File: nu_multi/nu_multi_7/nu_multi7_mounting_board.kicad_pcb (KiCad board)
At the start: 2 copper layers, 82.5 x 18.2 mm, 16 parts, among them J1 CONN_01X02, J10 CONN_01X03, J11 CONN_01X02, J12 CONN_01X03, J13 CONN_01X02, J14 CONN_01X03, J15 CONN_01X14, J2 CONN_01X03, J3 CONN_01X02, J4 CONN_01X02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

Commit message: Updates; added nu multi-8 mounting board
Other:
- board text added: "v2.5"

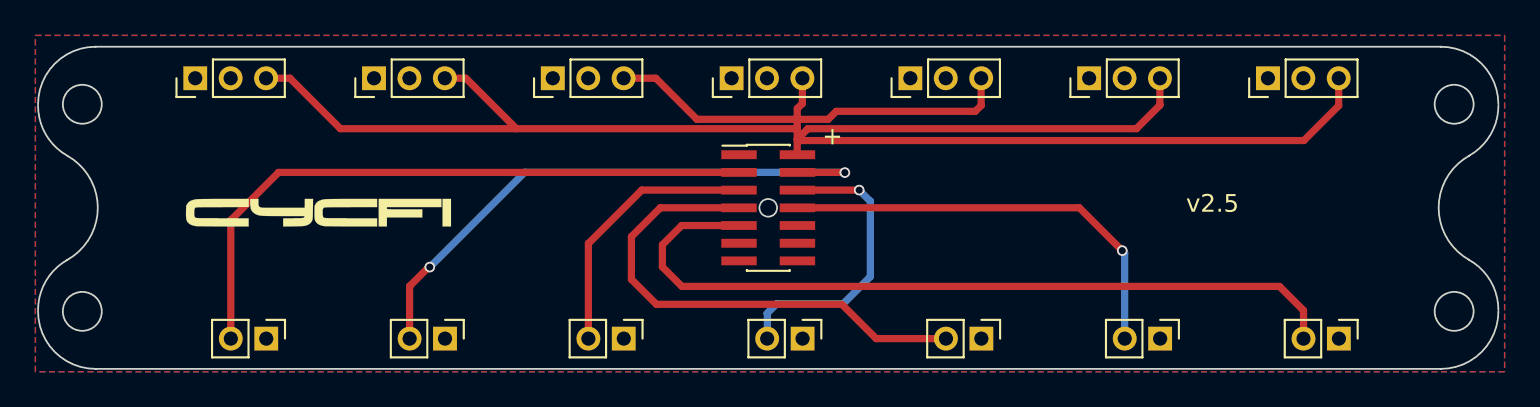
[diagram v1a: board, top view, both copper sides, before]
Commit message: Upgraded schematics and PCB layout using Nu Capsule footprint
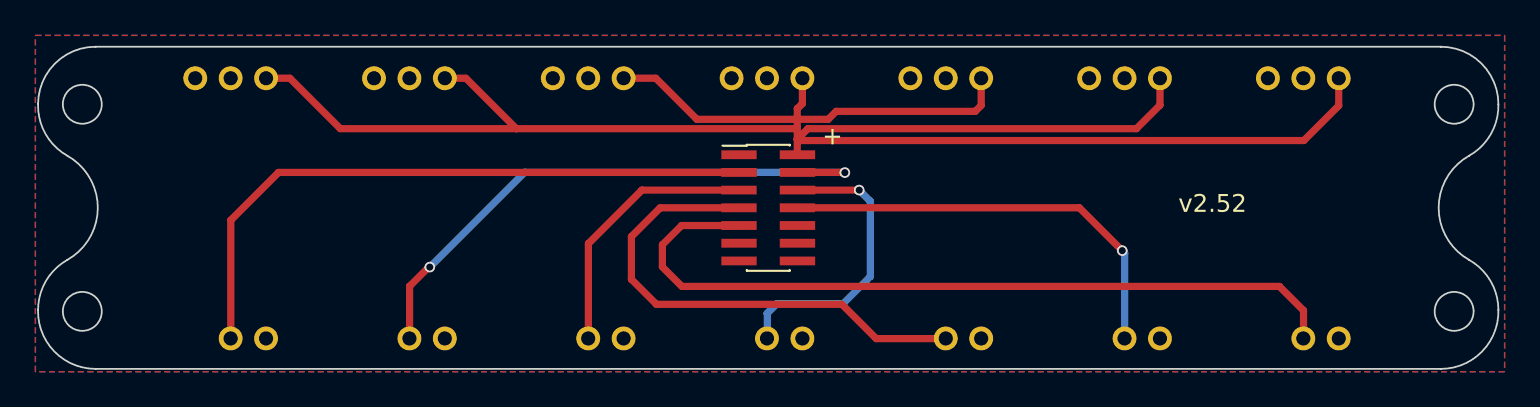
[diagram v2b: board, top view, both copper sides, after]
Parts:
- removed G***: LOGO, Symbols:Cycfi_Logo
- removed J1, J11, J13, J3, J4, J7, J9: CONN_01X02, Pin_Headers:Pin_Header_Straight_1x02_Pitch2.00mm
- removed J10, J12, J14, J2, J5, J6, J8: CONN_01X03, Pin_Headers:Pin_Header_Straight_1x03_Pitch2.00mm
- added U1: nu_capsule, cycfi_library:nu_capsule, F.Cu at (116.0, 62.4)
- added U2: nu_capsule, cycfi_library:nu_capsule, F.Cu at (126.1, 62.4)
- added U3: nu_capsule, cycfi_library:nu_capsule, F.Cu at (136.2, 62.4)
- added U4: nu_capsule, cycfi_library:nu_capsule, F.Cu at (146.3, 62.4)
- added U5: nu_capsule, cycfi_library:nu_capsule, F.Cu at (156.4, 62.4)
- added U6: nu_capsule, cycfi_library:nu_capsule, F.Cu at (166.5, 62.4)
- added U7: nu_capsule, cycfi_library:nu_capsule, F.Cu at (176.6, 62.4)
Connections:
- J15 pad 10: Net-(J15-Pad10) -> unconnected-(J15-Pad10)
- J15 pad 3: Net-(J13-Pad2) -> CH1
- J15 pad 4: Net-(J11-Pad2) -> CH2
- J15 pad 5: Net-(J15-Pad5) -> CH3
- J15 pad 6: Net-(J15-Pad6) -> CH4
- J15 pad 7: Net-(J15-Pad7) -> CH5
- J15 pad 8: Net-(J15-Pad8) -> CH6
- J15 pad 9: Net-(J1-Pad2) -> CH7
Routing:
- net CH7: track 0.00 -> 44.9 mm
- net Net-(J1-Pad2): track 44.9 -> 0.00 mm
- net Net-(J13-Pad2): track 36.5 -> 0.00 mm
- net CH1: track 0.00 -> 36.5 mm
- net Net-(J11-Pad2): track 32.9 -> 0.00 mm, vias 2 -> 0
- net CH2: track 0.00 -> 32.9 mm, vias 0 -> 2
- net Net-(J15-Pad7): track 28.3 -> 0.00 mm
- net CH5: track 0.00 -> 28.3 mm
- net Net-(J15-Pad8): track 24.4 -> 0.00 mm, vias 1 -> 0
- net CH6: track 0.00 -> 24.4 mm, vias 0 -> 1
- net Net-(J15-Pad6): track 16.8 -> 0.00 mm, vias 1 -> 0
- net CH4: track 0.00 -> 16.8 mm, vias 0 -> 1
- net Net-(J15-Pad5): track 15.1 -> 0.00 mm
- net CH3: track 0.00 -> 15.1 mm
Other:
- outline, holes or cut-outs redrawn
- net class Default removed
- board text added: "v2.52"
- board text removed: "v2.5"

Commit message: Use 2x7p connector from cycfi lib
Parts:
- J15: footprint Pin_Headers:Pin_Header_Straight_2x07_Pitch1.00mm_SMD -> cycfi_library:pin_header_2x7p_1.00mm_smd_vertical

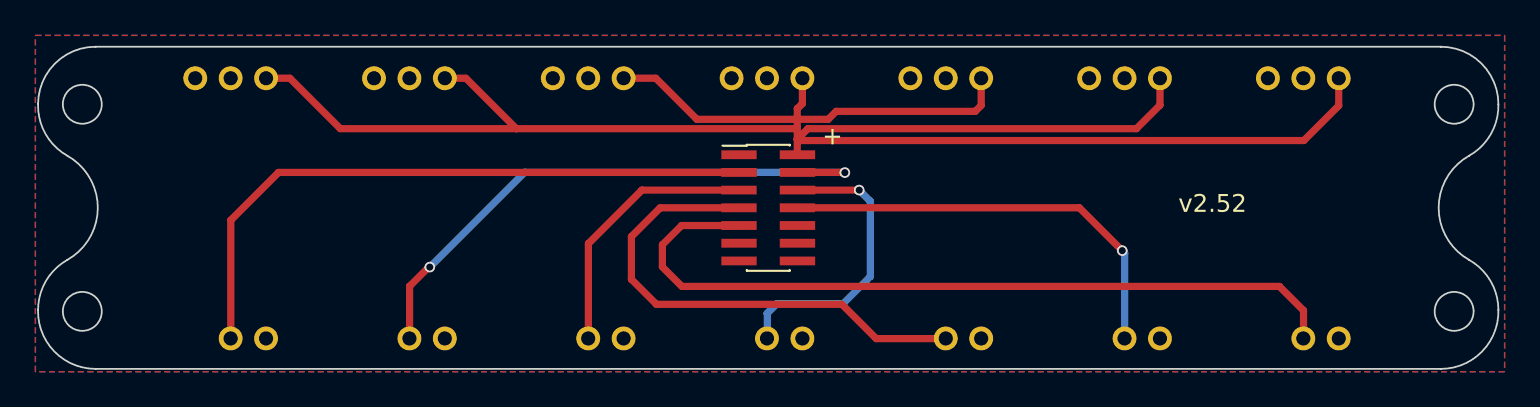
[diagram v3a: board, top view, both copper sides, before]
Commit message: - Fix wrong string spacing - Bump to v2.54
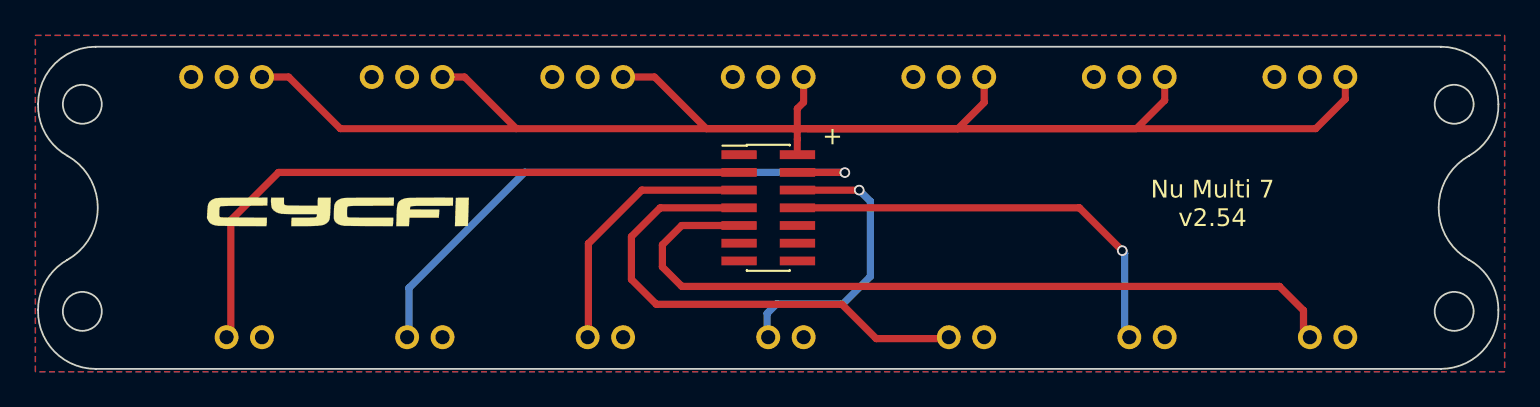
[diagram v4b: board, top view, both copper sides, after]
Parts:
- added G***: LOGO, cycfi_library:cycfi-logo-15mm, F.Cu at (124.0, 70.0)
- moved U7 0.38 mm to (177.0, 62.4)
- moved U6 0.28 mm to (166.8, 62.4)
- moved U1 0.24 mm to (115.8, 62.4)
- moved U5 0.18 mm to (156.6, 62.4)
- moved U2 0.15 mm to (126.0, 62.4)
- moved U4 0.10 mm to (146.4, 62.4)
- moved U3 0.08 mm to (136.2, 62.4)
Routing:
- net V+: track 119.7 -> 120.3 mm
- net CH2: vias 2 -> 1
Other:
- board text added: "Nu Multi 7 v2.54"
- board text removed: "v2.52"
